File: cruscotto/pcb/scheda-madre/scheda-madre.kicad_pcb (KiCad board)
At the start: 4 copper layers, 178.7 x 74 mm, 149 parts, among them J1 Micro-Fit 2x12 verso auto (D-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, J10 Verso P1 S3: 5V TXD RXD GND, J11 Verso P2 S3: IO19 IO11 IO12 I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, J12 Verso P6 Speak S3, J3 USB-C (solo a banco), J4 Ventola Delta AFB0412VA-00 (D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, J5 NTC display, J6 STEVAL-MKI196V1 (DIL-24), J7 Modulo MicroSD: 3V3 CS MOSI C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, J8 Modulo VAN: 3.3V GND RX TX, J9 Modulo VAN: CANH CANL, K1 G2RL-2 DC5, K2 G2RL-2 DC5, Q1 IPD50N06S4L-12, Q3 ZXMP6A13F (P 60 V), Q4 MMBTA06 (80 V), Q5 MMBT3904, Q6 MMBT3904, Q7 MMBT3904, Q8 MMBT5551, Q9 AO3400A, SW3 RESET, SW4 BOOT, U1 LM74700-Q1, U10 DS3231SN, U2 TPS54360B, U3 LMR36510, U4 ESP32-WROOM-32E-H4, U5 AP2112K-3.3, U6 CH340C, U7 LM2903B, U9 AP2112K-3.3

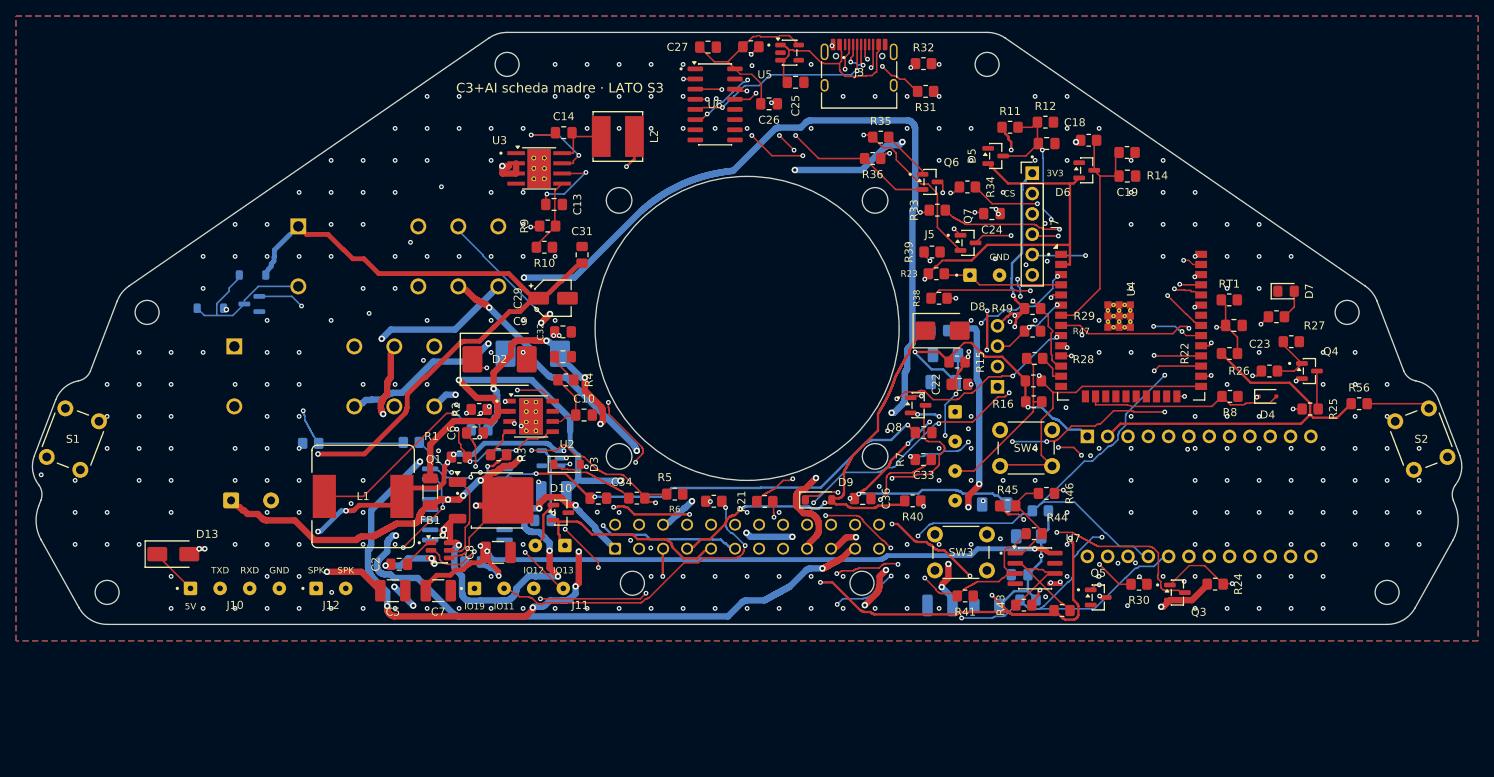
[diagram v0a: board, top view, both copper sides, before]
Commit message: feat(pcb): D-061 contorno v3 (+15 mm in basso) e J1 Micro-Fit verticale 43045-2412
Contorno motherboard_v3.DXF dell'utente (178,7 x 89 mm, fori invariati), J1 verticale
al centro della nuova fascia, piazzamento e sbroglio rifatti: 0 errori DRC, 0 non connessi.
Liste acquisti: J1 da Farnell 1012244, tolto C277384 da LCSC. Ingombro 3D di J1 con spina.

Co-Authored-By: Claude Opus 5.5 <noreply@anthropic.com>
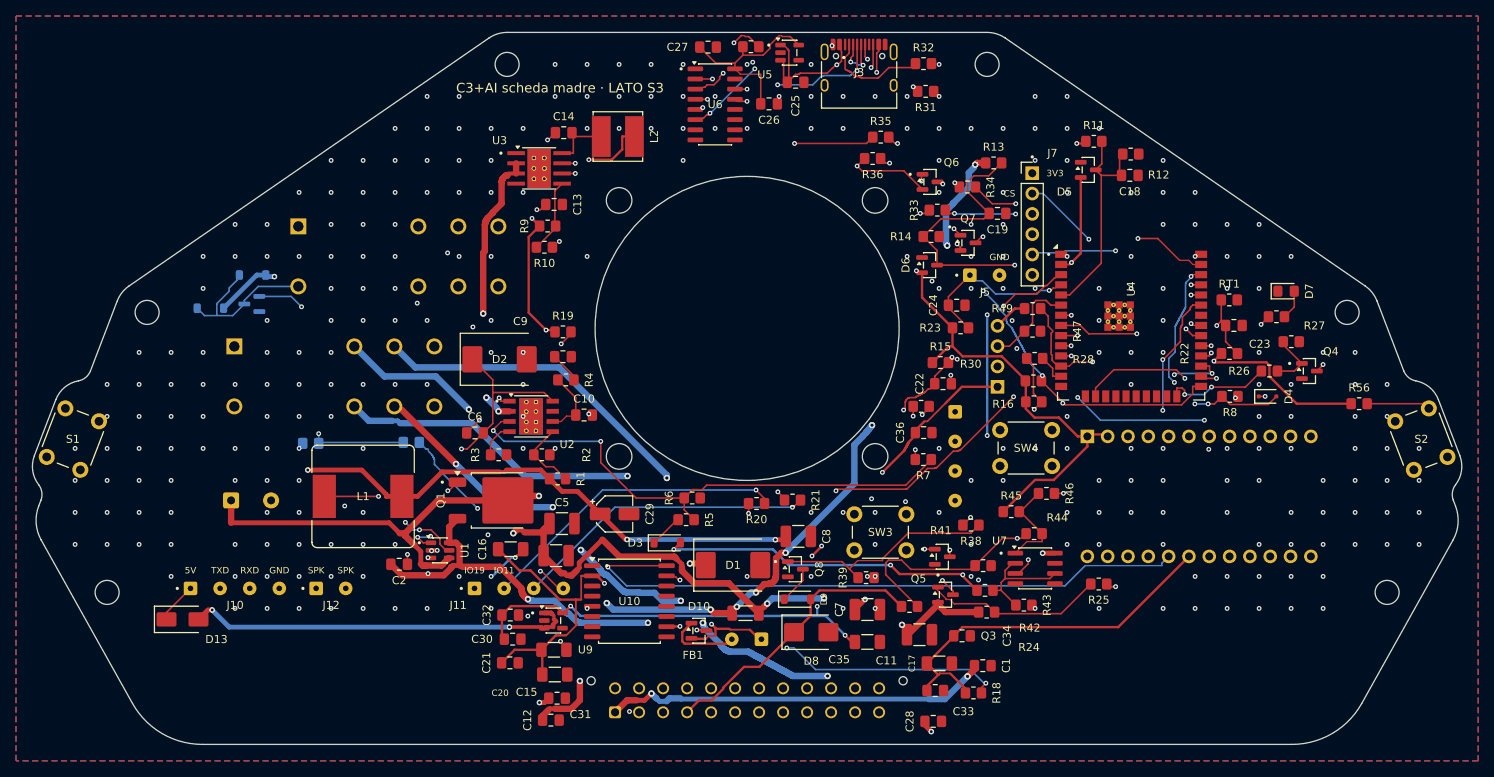
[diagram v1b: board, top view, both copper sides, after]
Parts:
- C1, C11, C12, C15, C16, C17, C20, C21, C28, C30, C35, C4, D1, R18, R19, U10, U9: moved to F.Cu
- J1: value Micro-Fit 2x12 verso auto (D-044) -> Micro-Fit 2x12 verticale verso auto (D-061); footprint Molex_Micro-Fit_3.0_43045-2400_2x12_P3.00mm_Horizontal -> Molex_Micro-Fit_3.0_43045-2412_2x12_P3.00mm_Vertical
- moved C1 69.5 mm to (178.0, 147.2), turned to 0 degrees
- moved C12 68.8 mm to (124.0, 154.0), turned to 0 degrees
- moved R19 67.1 mm to (125.5, 105.4), turned to 0 degrees
- moved C21 64.7 mm to (118.8, 146.8), turned to 0 degrees
- moved C15 61.7 mm to (124.5, 148.3), turned to 0 degrees
- moved C28 60.9 mm to (171.8, 154.1), turned to 0 degrees
- moved C16 59.5 mm to (118.9, 132.6), turned to 0 degrees
- moved C20 59.1 mm to (124.4, 145.2), turned to 0 degrees
- moved C31 55.5 mm to (124.7, 151.2), turned to 0 degrees
- moved C7 53.7 mm to (163.5, 140.1)
- moved C34 48.6 mm to (175.4, 143.4)
- moved FB1 42.2 mm to (148.3, 140.6), turned to 0 degrees
- moved R39 41.5 mm to (163.4, 136.2)
- moved D8 41.1 mm to (156.5, 143.0)
- moved C8 37.6 mm to (154.9, 131.0)
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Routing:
- net +12V_F: track 272.6 -> 153.4 mm, vias 11 -> 8
- net RADIO_L_N: track 148.2 -> 76.6 mm, vias 4 -> 1
- net KEY_IN: track 191.2 -> 125.3 mm, vias 12 -> 6
- net I2C_SDA: track 149.9 -> 107.5 mm, vias 9 -> 5
- net Net-(Q4-C): track 4.81 -> 46.9 mm, vias 0 -> 2
- net LINK_S32FE: track 70.1 -> 37.9 mm, vias 5 -> 1
- net +3V3_SW: track 155.9 -> 125.4 mm, vias 10 -> 6
- net +3V3_AON: track 323.5 -> 352.7 mm, vias 10 -> 7
- net SPK_R_N: track 44.2 -> 73.0 mm, vias 3 -> 0
- net SPK_L_P: track 105.7 -> 78.9 mm, vias 6 -> 1
- net SPK_R_P: track 48.5 -> 72.9 mm, vias 3 -> 0
- net Net-(D9-K): track 27.4 -> 4.71 mm, vias 2 -> 0
- net GND: track 29.9 -> 12.0 mm, vias 315 -> 310
- net KLINE: track 52.6 -> 35.2 mm, vias 2 -> 0
- net VBAT_SENSE: track 29.2 -> 45.8 mm, vias 0 -> 2
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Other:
- board size 178.7 x 74 mm -> 178.7 x 89 mm
- board text removed: "​IO12"
- board text removed: "​IO13"

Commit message: feat(pcb): J1 sotto la ventola, nella parte più profonda del vano (D-061); sbroglio rifatto, DRC 0/0
Co-Authored-By: Claude Opus 5.5 <noreply@anthropic.com>
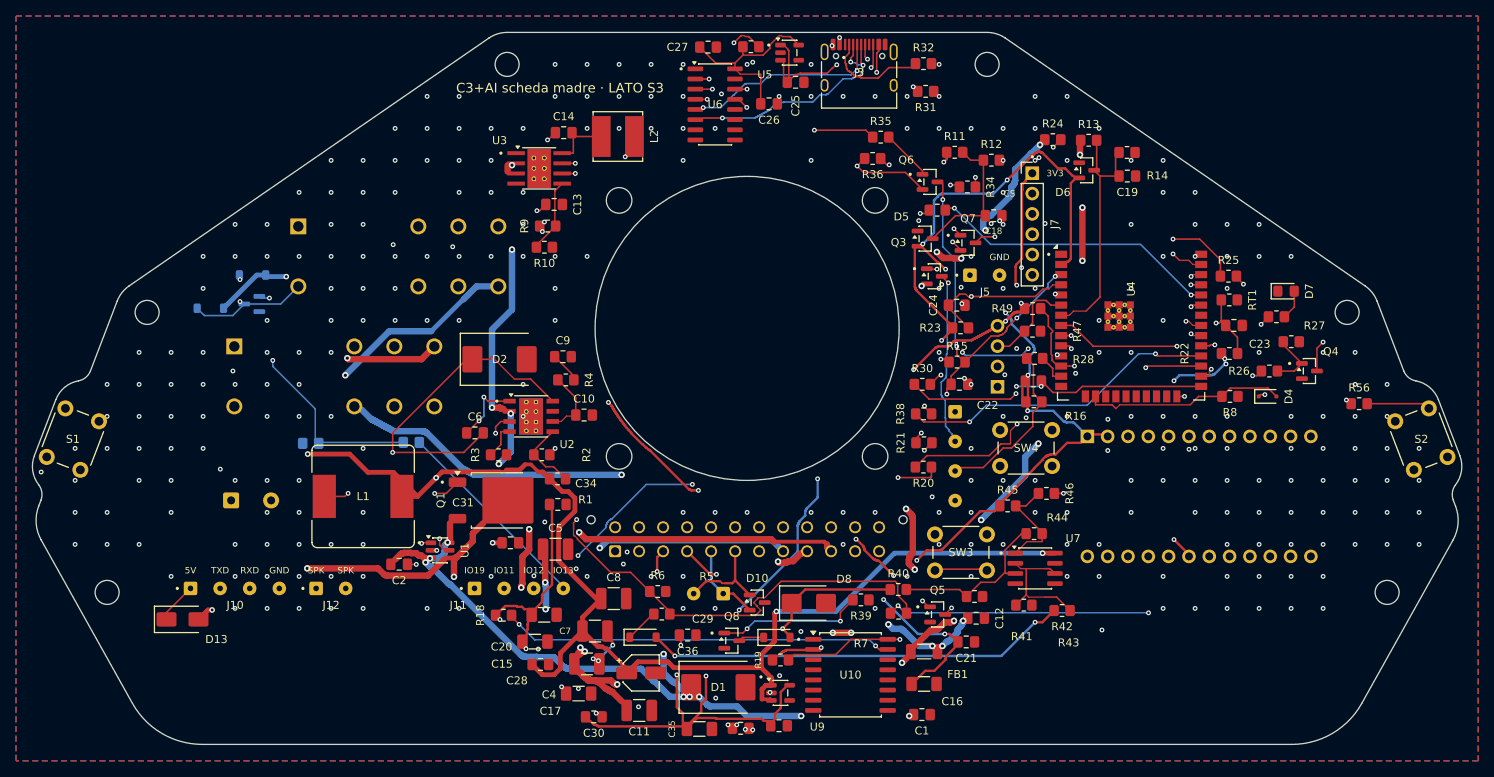
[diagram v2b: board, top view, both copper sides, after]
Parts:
- moved R24 59.6 mm to (186.7, 81.4)
- moved R18 59.5 mm to (118.1, 140.9)
- moved C21 57.1 mm to (175.9, 144.2)
- moved C12 54.7 mm to (177.1, 141.2)
- moved C16 54.4 mm to (170.6, 149.4)
- moved C34 53.1 mm to (124.8, 127.0)
- moved C28 49.6 mm to (122.7, 147.0)
- moved R19 49.2 mm to (152.7, 146.4)
- moved C17 45.2 mm to (127.4, 150.6)
- moved R25 41.8 mm to (208.7, 98.5)
- moved Q3 39.8 mm to (171.9, 98.5)
- moved C36 38.9 mm to (141.1, 143.3)
- moved C32 36.3 mm to (152.5, 154.7)
- moved C11 36.3 mm to (135.0, 152.8)
- moved C7 34.2 mm to (129.5, 142.8)
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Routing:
- net +12V_F: track 153.4 -> 216.3 mm, vias 8 -> 25
- net I2C_SCL: track 149.8 -> 101.1 mm, vias 4 -> 2
- net Net-(Q3-G): track 22.5 -> 61.6 mm, vias 0 -> 3
- net LINK_S32FE: track 37.9 -> 72.8 mm
- net SPK_R_N: track 73.0 -> 40.8 mm
- net RADIO_R_N: track 70.6 -> 41.7 mm
- net Net-(Q4-C): track 46.9 -> 18.2 mm
- net VBAT_P: track 155.4 -> 180.5 mm
- net Net-(Q8-B): track 28.2 -> 52.2 mm, vias 0 -> 3
- net SPK_R_P: track 72.9 -> 50.7 mm
- net +5V: track 258.2 -> 236.3 mm, vias 10 -> 7
- net VBAT_IN: track 120.2 -> 98.5 mm, vias 7 -> 9
- net FE_TX: track 50.9 -> 29.6 mm, vias 4 -> 2
- net LINK_FE2S3: track 38.7 -> 59.6 mm, vias 1 -> 3
- net I2C_SDA: track 107.5 -> 127.9 mm, vias 5 -> 3
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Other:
- board text added: "​IO12"
- board text added: "​IO13"
